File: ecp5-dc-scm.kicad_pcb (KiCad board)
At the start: 6 copper layers, 90 x 120.4 mm, 189 parts, among them IC1 TPS54561, J1 WE-RJ45_7499111121A, J10 61300611121, J2 1-2199230-6, J3 543630489, J4 M20-7830642, J5 SFF-TA-1002-4C+, J6 2X05, J7 61301021121, J8 61301021121, J9 61301221121, U1 KSZ9031RNXCA, U10 LM21212-2, U14 TPS62823DLCT, U15 TPS62823DLCT, U16 TPS62823DLCT, U17 TPS62823DLCT, U18 ECP5UM5G_85_CABGA756, U2 W25Q32JVSSIQ_TR, U3 W25Q32JVSSIQ_TR, U4 W25Q32JVSSIQ_TR, U5 W25Q32JVSSIQ_TR, U6 NVT2008DQ,115, U7 AS4C256M16D3, U8 TPS51200DRC, Y1 ABM8G-25.000MHZ-18-D2Y-T

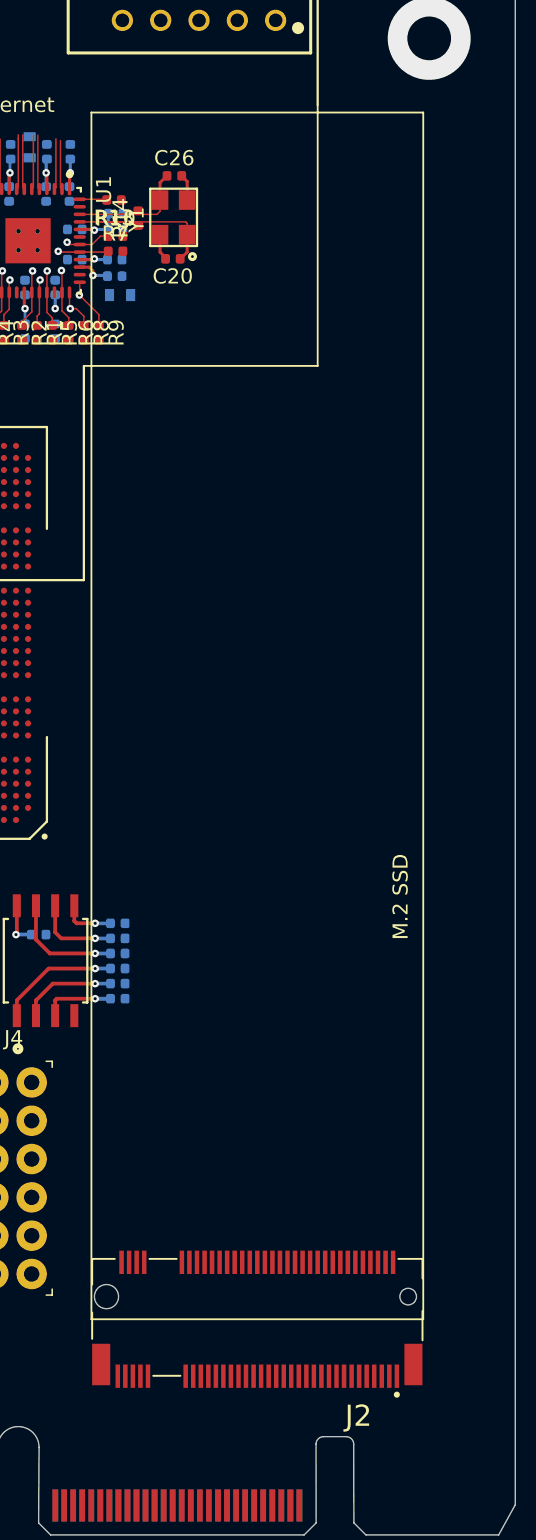
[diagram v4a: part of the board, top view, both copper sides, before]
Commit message: Add PCIe passives placement
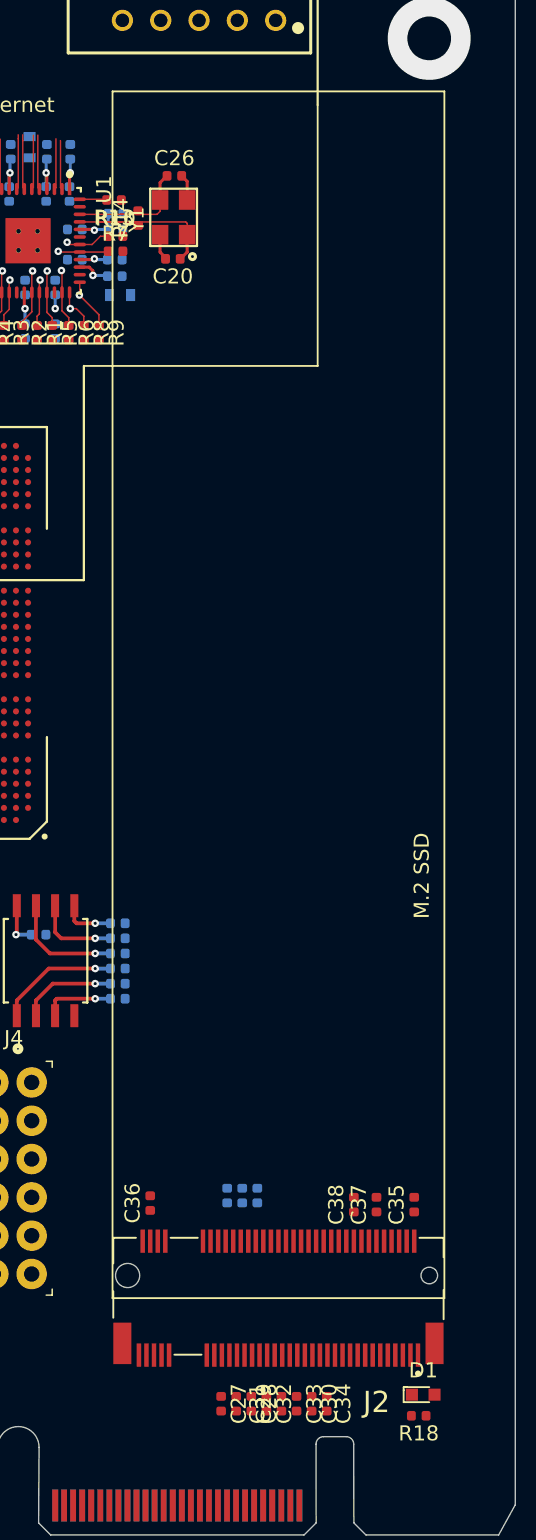
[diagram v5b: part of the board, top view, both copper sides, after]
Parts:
- added C27: C_100n_0402, ecp5-dc-scm-footprints:0402-cap, F.Cu at (130.6, 170.6)
- added C28: C_100n_0402, ecp5-dc-scm-footprints:0402-cap, F.Cu at (132.6, 170.6)
- added C29: C_100n_0402, ecp5-dc-scm-footprints:0402-cap, F.Cu at (134.6, 170.6)
- added C30: C_100n_0402, ecp5-dc-scm-footprints:0402-cap, F.Cu at (136.6, 170.6)
- added C31: C_100n_0402, ecp5-dc-scm-footprints:0402-cap, F.Cu at (131.6, 170.6)
- added C32: C_100n_0402, ecp5-dc-scm-footprints:0402-cap, F.Cu at (133.6, 170.6)
- added C33: C_100n_0402, ecp5-dc-scm-footprints:0402-cap, F.Cu at (135.6, 170.6)
- added C34: C_100n_0402, ecp5-dc-scm-footprints:0402-cap, F.Cu at (137.6, 170.6)
- added C35: C_10u_0402, ecp5-dc-scm-footprints:0402-cap, F.Cu at (143.4, 157.4)
- added C36: C_10u_0402, ecp5-dc-scm-footprints:0402-cap, F.Cu at (125.9, 157.3)
- added C37: C_10u_0402, ecp5-dc-scm-footprints:0402-cap, F.Cu at (140.9, 157.4)
- added C38: C_10u_0402, ecp5-dc-scm-footprints:0402-cap, F.Cu at (139.4, 157.4)
- added D1: KP-1608CGCK, ecp5-dc-scm-footprints:LED_0603, F.Cu at (144.0, 170.0)
- added R17: R_10k_0402, ecp5-dc-scm-footprints:0402-res, B.Cu at (131.0, 156.8)
- added R18: R_330R_0402, ecp5-dc-scm-footprints:0402-res, F.Cu at (143.7, 171.4)
- added R19: R_10k_0402, ecp5-dc-scm-footprints:0402-res, B.Cu at (132.0, 156.8)
- added R20: R_10k_0402, ecp5-dc-scm-footprints:0402-res, B.Cu at (133.0, 156.8)
- moved J2 1.98 mm to (134.4, 162.1)

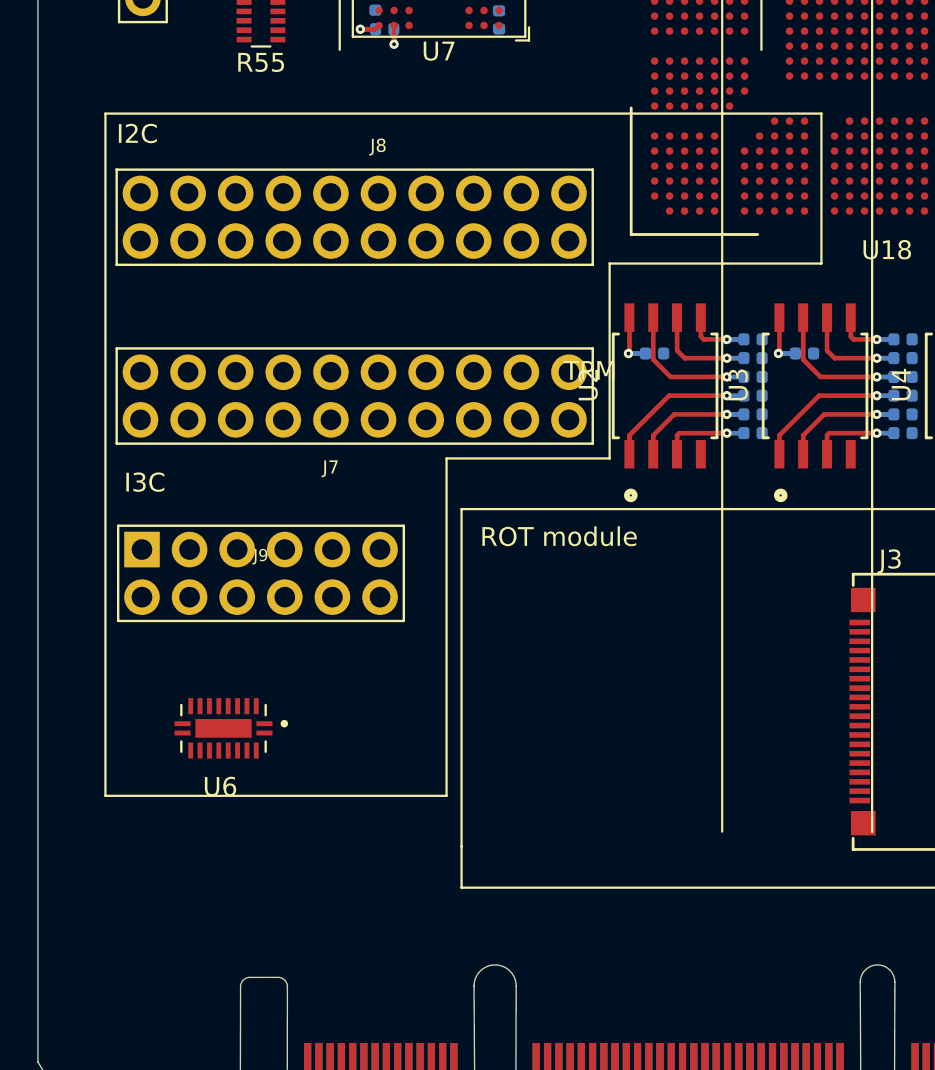
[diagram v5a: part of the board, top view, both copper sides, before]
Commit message: Remove I2C and I3C goldpin connectors
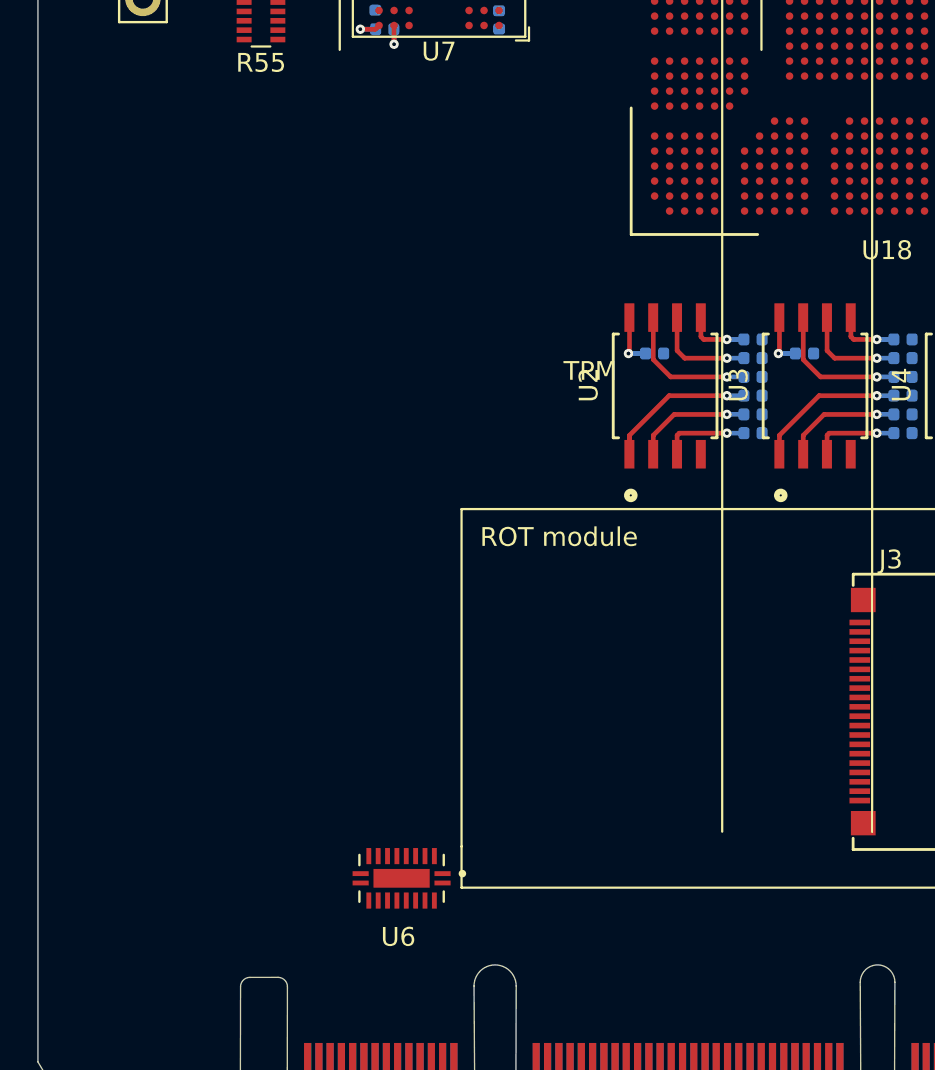
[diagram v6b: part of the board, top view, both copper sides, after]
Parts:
- removed J7, J8: 61301021121, ecp5-dc-scm-footprints:61301021121
- removed J9: 61301221121, ecp5-dc-scm-footprints:61301221121
- moved U6 12.4 mm to (79.5, 167.5)
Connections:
- J5 pad OA10: I3C[2]_SDA -> I3C[2]_SDA_1V0
- J5 pad OA11: I3C[3]_SCL -> I3C[3]_SCL_1V0
- J5 pad OA12: I3C[3]_SDA -> I3C[3]_SDA_1V0
- J5 pad OA5: I3C[0]_SCL -> I3C[0]_SCL_1V0
- J5 pad OA6: I3C[0]_SDA -> I3C[0]_SDA_1V0
- J5 pad OA7: I3C[1]_SCL -> I3C[1]_SCL_1V0
- J5 pad OA8: I3C[1]_SDA -> I3C[1]_SDA_1V0
- J5 pad OA9: I3C[2]_SCL -> I3C[2]_SCL_1V0
- U6 pad 10: I3C[3]_SCL_3V3 -> I3C[0]_SCL_3V3
- U6 pad 11: I3C[3]_SCL_1V0 -> I3C[0]_SCL_1V0
- U6 pad 12: I3C[3]_SDA_1V0 -> I3C[0]_SDA_1V0
- U6 pad 13: I3C[2]_SCL_1V0 -> I3C[1]_SCL_1V0
- U6 pad 14: I3C[2]_SDA_1V0 -> I3C[1]_SDA_1V0
- U6 pad 15: I3C[1]_SCL_1V0 -> I3C[2]_SCL_1V0
- U6 pad 16: I3C[1]_SDA_1V0 -> I3C[2]_SDA_1V0
- U6 pad 17: I3C[0]_SCL_1V0 -> I3C[3]_SCL_1V0
- U6 pad 18: I3C[0]_SDA_1V0 -> I3C[3]_SDA_1V0
- U6 pad 3: I3C[0]_SDA_3V3 -> I3C[3]_SDA_3V3
- U6 pad 4: I3C[0]_SCL_3V3 -> I3C[3]_SCL_3V3
- U6 pad 5: I3C[1]_SDA_3V3 -> I3C[2]_SDA_3V3
- U6 pad 6: I3C[1]_SCL_3V3 -> I3C[2]_SCL_3V3
- U6 pad 7: I3C[2]_SDA_3V3 -> I3C[1]_SDA_3V3
- U6 pad 8: I3C[2]_SCL_3V3 -> I3C[1]_SCL_3V3
- U6 pad 9: I3C[3]_SDA_3V3 -> I3C[0]_SDA_3V3
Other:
- board text removed: "I2C"
- board text removed: "I3C"

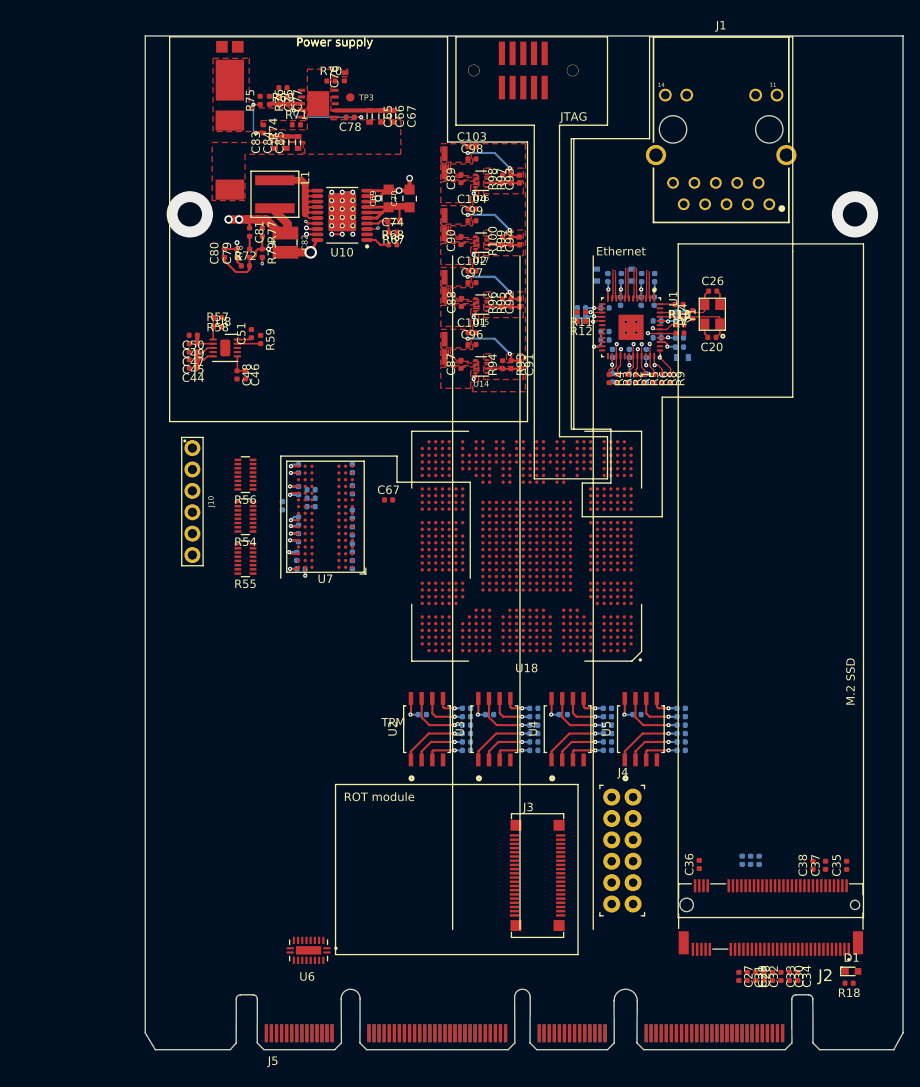
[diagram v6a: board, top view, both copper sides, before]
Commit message: Add power supply component placement -WIP
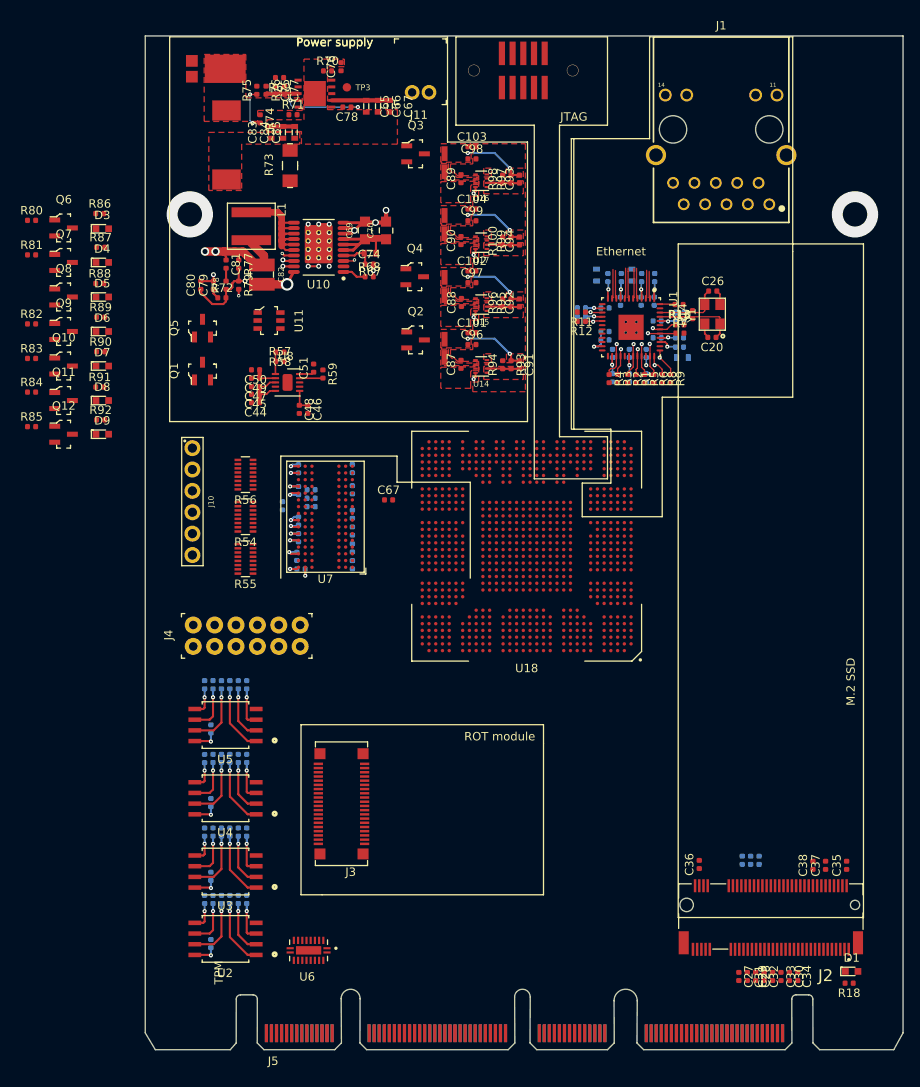
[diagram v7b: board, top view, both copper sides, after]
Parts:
- added D3: LG_L29K-G2J1-24-Z, ecp5-dc-scm-footprints:LED_0603, F.Cu at (55.0, 81.8)
- added D4: LG_L29K-G2J1-24-Z, ecp5-dc-scm-footprints:LED_0603, F.Cu at (55.0, 85.8)
- added D5: LG_L29K-G2J1-24-Z, ecp5-dc-scm-footprints:LED_0603, F.Cu at (55.0, 89.9)
- added D6: LG_L29K-G2J1-24-Z, ecp5-dc-scm-footprints:LED_0603, F.Cu at (55.0, 94.0)
- added D7: LG_L29K-G2J1-24-Z, ecp5-dc-scm-footprints:LED_0603, F.Cu at (55.0, 98.1)
- added D8: LG_L29K-G2J1-24-Z, ecp5-dc-scm-footprints:LED_0603, F.Cu at (55.0, 102.2)
- added D9: LG_L29K-G2J1-24-Z, ecp5-dc-scm-footprints:LED_0603, F.Cu at (55.0, 106.2)
- added J11: S2B-PH-K-S_LF__SN_, ecp5-dc-scm-footprints:PinHeader_1x2_P2mm_Drill1mm_RA, F.Cu at (93.8, 65.6)
- added Q1: IRLML6402TRPBF, ecp5-dc-scm-footprints:SOT-23-3, F.Cu at (66.9, 98.7)
- added Q10: 2N7002, ecp5-dc-scm-footprints:SOT-23-3, F.Cu at (50.4, 98.1)
- added Q11: 2N7002, ecp5-dc-scm-footprints:SOT-23-3, F.Cu at (50.4, 102.2)
- added Q12: 2N7002, ecp5-dc-scm-footprints:SOT-23-3, F.Cu at (50.4, 106.2)
- added Q2: IRLML6402TRPBF, ecp5-dc-scm-footprints:SOT-23-3, F.Cu at (92.2, 95.0)
- added Q3: IRLML6402TRPBF, ecp5-dc-scm-footprints:SOT-23-3, F.Cu at (92.2, 72.9)
- added Q4: IRLML6402TRPBF, ecp5-dc-scm-footprints:SOT-23-3, F.Cu at (92.1, 87.5)
- added Q5: IRLML6402TRPBF, ecp5-dc-scm-footprints:SOT-23-3, F.Cu at (66.9, 93.6)
- added Q6: 2N7002, ecp5-dc-scm-footprints:SOT-23-3, F.Cu at (50.4, 81.7)
- added Q7: 2N7002, ecp5-dc-scm-footprints:SOT-23-3, F.Cu at (50.4, 85.8)
- added Q8: 2N7002, ecp5-dc-scm-footprints:SOT-23-3, F.Cu at (50.4, 89.9)
- added Q9: 2N7002, ecp5-dc-scm-footprints:SOT-23-3, F.Cu at (50.4, 94.0)
- added R73: R_0R_1206, antmicro-footprints:1206-res, F.Cu at (77.3, 74.3)
- added R80: R_10k_0402, ecp5-dc-scm-footprints:0402-res, F.Cu at (46.6, 80.8)
- added R81: R_10k_0402, ecp5-dc-scm-footprints:0402-res, F.Cu at (46.6, 84.9)
- added R82: R_10k_0402, ecp5-dc-scm-footprints:0402-res, F.Cu at (46.6, 93.1)
- added R83: R_10k_0402, ecp5-dc-scm-footprints:0402-res, F.Cu at (46.6, 97.2)
- added R84: R_10k_0402, ecp5-dc-scm-footprints:0402-res, F.Cu at (46.6, 101.2)
- added R85: R_10k_0402, ecp5-dc-scm-footprints:0402-res, F.Cu at (46.6, 105.3)
- added R86: R_1k_0402, ecp5-dc-scm-footprints:0402-res, F.Cu at (54.7, 80.0)
- added R87: R_1k_0402, ecp5-dc-scm-footprints:0402-res, F.Cu at (54.8, 84.0)
- added R88: R_1k_0402, ecp5-dc-scm-footprints:0402-res, F.Cu at (54.7, 88.3)
- added R89: R_1k_0402, ecp5-dc-scm-footprints:0402-res, F.Cu at (54.8, 92.3)
- added R90: R_1k_0402, ecp5-dc-scm-footprints:0402-res, F.Cu at (54.8, 96.4)
- added R91: R_1k_0402, ecp5-dc-scm-footprints:0402-res, F.Cu at (54.7, 100.6)
- added R92: R_1k_0402, ecp5-dc-scm-footprints:0402-res, F.Cu at (54.8, 104.5)
- added U11: SN74LVC1G11DBVR, ecp5-dc-scm-footprints:SOT-23-6, F.Cu at (74.8, 92.7)
- moved R32 56.7 mm to (67.2, 135.9), turned to 90 degrees
- moved R28 55.7 mm to (68.2, 135.9), turned to 270 degrees
- moved R40 54.8 mm to (69.2, 135.9), turned to 90 degrees
- moved R24 53.9 mm to (70.2, 135.9), turned to 270 degrees
- moved R44 53.0 mm to (71.2, 135.9), turned to 90 degrees
- moved J4 52.8 mm to (65.8, 131.4), turned to 90 degrees
- moved R36 52.2 mm to (72.2, 135.9), turned to 90 degrees
- moved C42 50.6 mm to (67.9, 141.2), turned to 90 degrees
- moved U5 49.3 mm to (69.6, 140.7), turned to 180 degrees
- moved R31 48.2 mm to (67.2, 144.7), turned to 90 degrees
- moved R27 47.1 mm to (68.2, 144.7), turned to 270 degrees
- moved R39 46.0 mm to (69.2, 144.7), turned to 90 degrees
- moved R23 44.9 mm to (70.2, 144.7), turned to 270 degrees
- moved R43 43.9 mm to (71.2, 144.7), turned to 90 degrees
- moved C41 43.1 mm to (67.9, 149.9), turned to 90 degrees
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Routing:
- net /Power supply/1V8_EN: track 0.00 -> 1.25 mm, vias 0 -> 3
- net (no net): track 32.5 -> 31.3 mm, vias 20 -> 17
